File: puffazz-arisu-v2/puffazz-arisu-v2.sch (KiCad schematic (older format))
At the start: 185 parts, among them SW1 SW_Push, U1 ATmega32U4-AU, Y1 16MHz

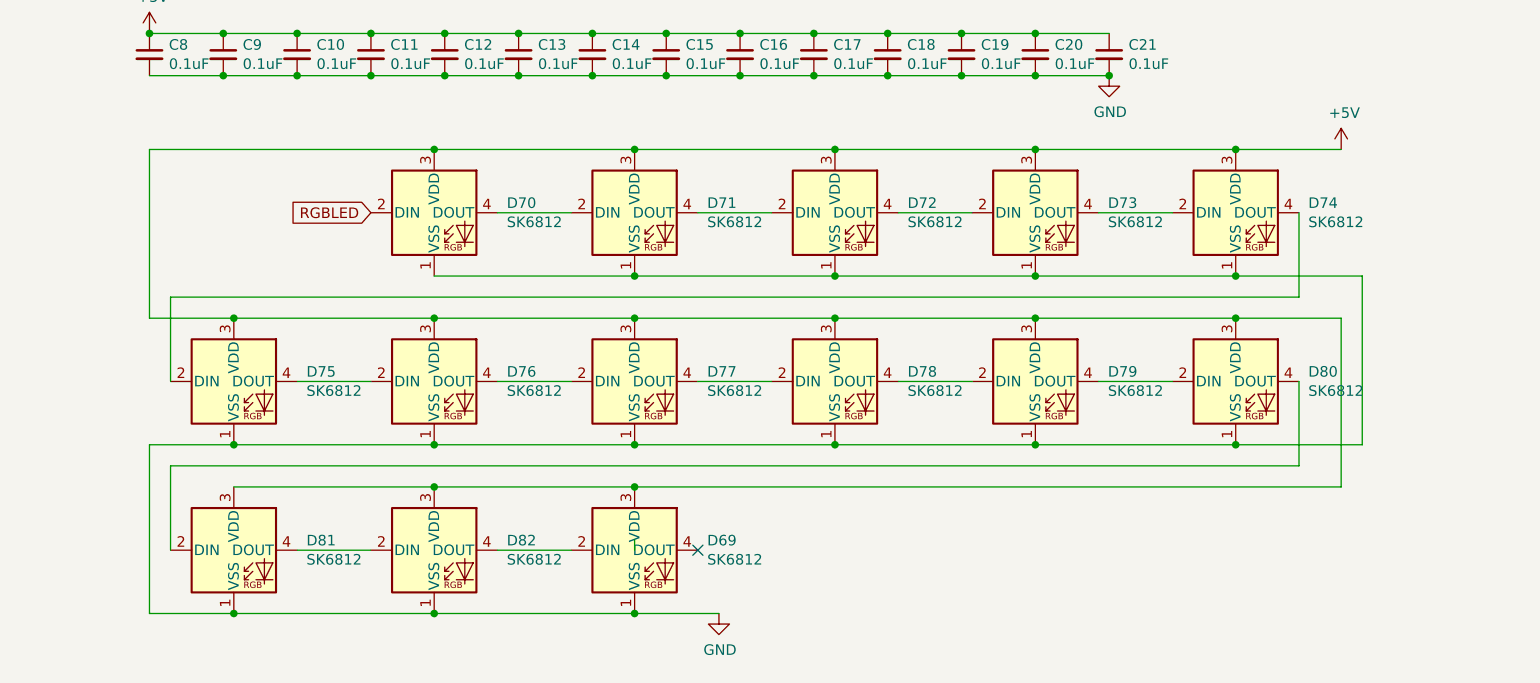
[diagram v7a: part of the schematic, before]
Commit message: Fixed small issues and swapped LED to WS2812B
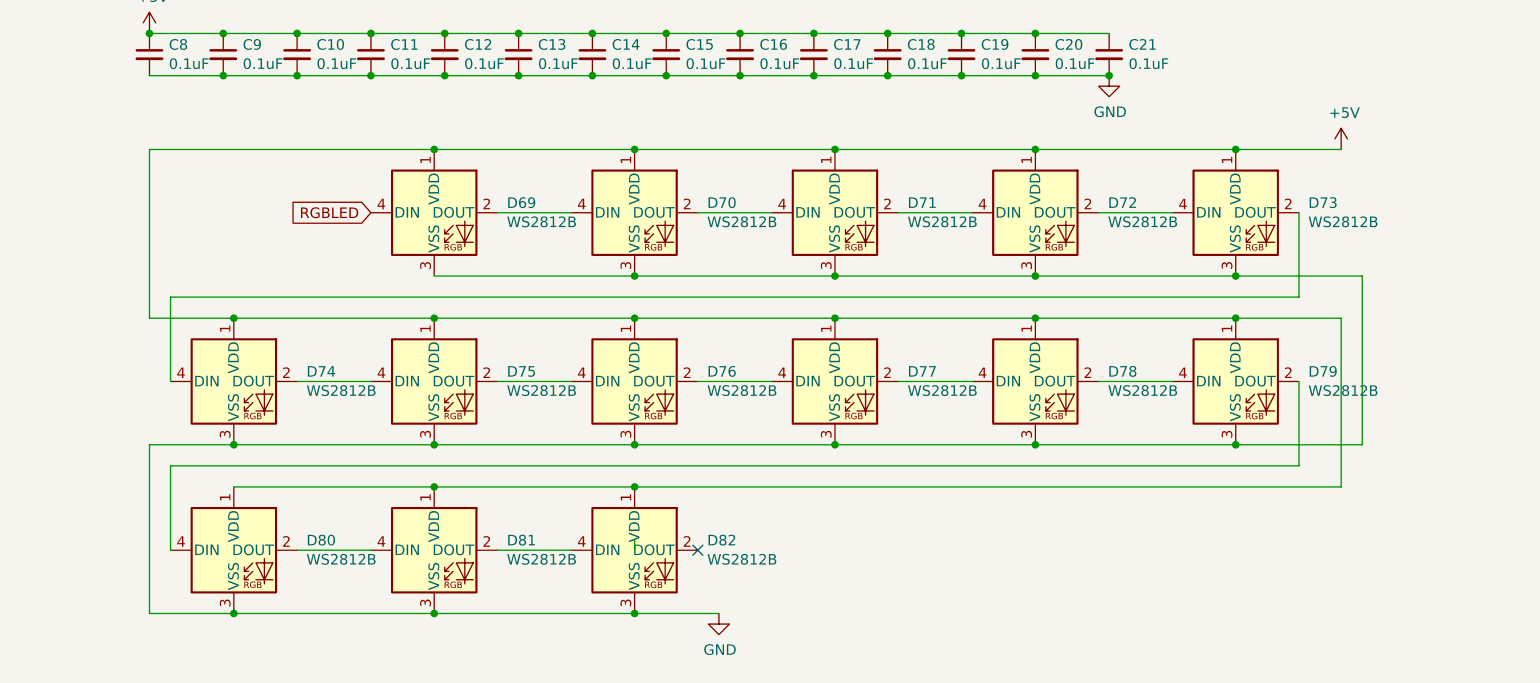
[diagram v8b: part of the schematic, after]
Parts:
- removed D69, D70, D71, D72, D73, D74, D75, D76, D77, D78, D79, D80, D81, D82: SK6812, LED_SMD:LED_SK6812_PLCC4_5.0x5.0mm_P3.2mm, symbol LED:SK6812
- added D69, D70, D71, D72, D73, D74, D75, D76, D77, D78, D79, D80, D81, D82: WS2812B, LED_SMD:LED_WS2812B_PLCC4_5.0x5.0mm_P3.2mm, symbol LED:WS2812B
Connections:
- net +5V: now also D69.1 (VDD), D70.1 (VDD), D71.1 (VDD), D72.1 (VDD), D73.1 (VDD), D74.1 (VDD), D75.1 (VDD), D76.1 (VDD), D77.1 (VDD), D78.1 (VDD), D79.1 (VDD), D80.1 (VDD), D81.1 (VDD), D82.1 (VDD)
- net GND: now also D69.3 (VSS), D70.3 (VSS), D71.3 (VSS), D72.3 (VSS), D73.3 (VSS), D74.3 (VSS), D75.3 (VSS), D76.3 (VSS), D77.3 (VSS), D78.3 (VSS), D79.3 (VSS), D80.3 (VSS), D81.3 (VSS), D82.3 (VSS)
- net RGBLED: now also D69.4 (DIN)
- new net: D69.2 (DOUT), D70.4 (DIN)
- new net: D70.2 (DOUT), D71.4 (DIN)
- new net: D71.2 (DOUT), D72.4 (DIN)
- new net: D72.2 (DOUT), D73.4 (DIN)
- new net: D73.2 (DOUT), D74.4 (DIN)
- new net: D74.2 (DOUT), D75.4 (DIN)
- new net: D75.2 (DOUT), D76.4 (DIN)
- new net: D76.2 (DOUT), D77.4 (DIN)
- new net: D77.2 (DOUT), D78.4 (DIN)
- new net: D78.2 (DOUT), D79.4 (DIN)
- new net: D79.2 (DOUT), D80.4 (DIN)
- new net: D80.2 (DOUT), D81.4 (DIN)
- new net: D81.2 (DOUT), D82.4 (DIN)
